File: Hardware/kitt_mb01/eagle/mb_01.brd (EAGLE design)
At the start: 160 x 100 mm, 123 parts, among them IC1.01 RT8293A, IC2.00 BQ24266RGET, IC3.01 LSM9DS1, U6.01 TPS61032RSARPSDO-G16, U7.01 SI1922EDH, U7.03 SI1922EDH, U7.2 SI1922EDH, X2.01 S2B-PH-K-S(LF)(SN), X7.02 ARDUINO_UNO, X7.03 CON_HEADER_1X02, X7.05 MOTOR, X7.06 CON_HEADER_1X02, X7.08 CON_HEADER_1X02, X7.09 0R-JUMPA, X7.10 0R-JUMPA, X7.11 CON_HEADER_1X02

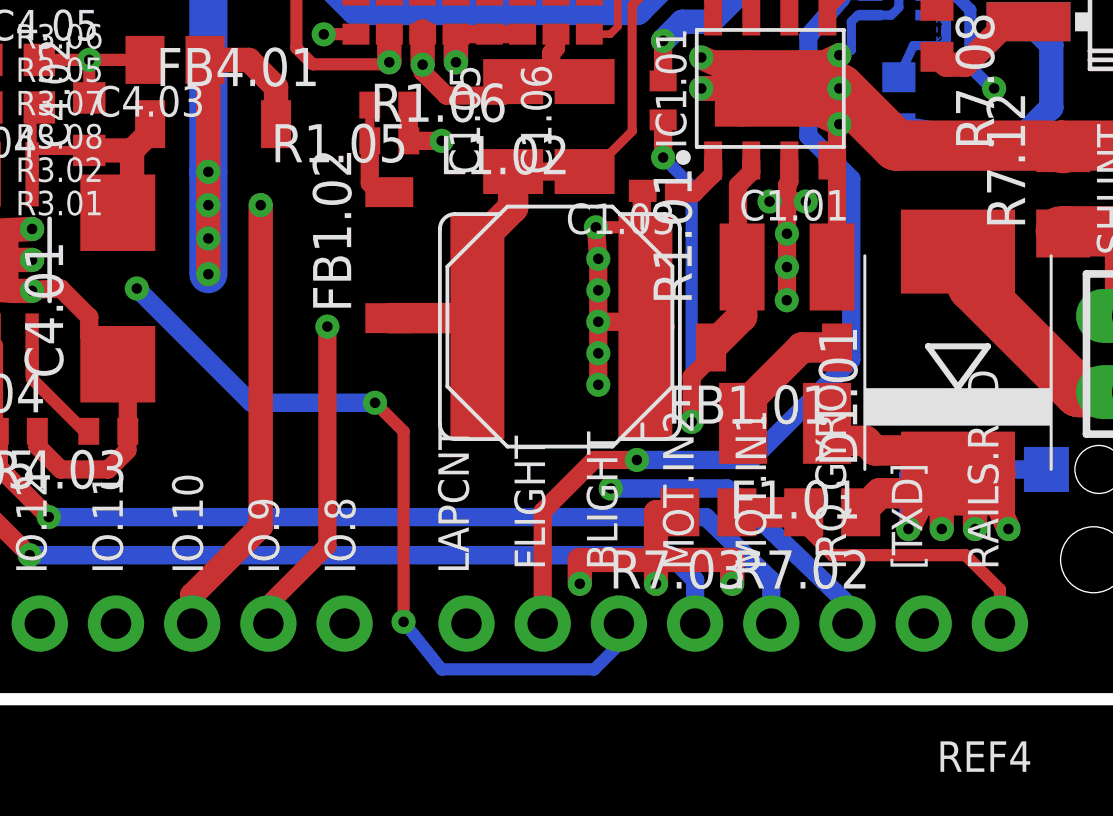
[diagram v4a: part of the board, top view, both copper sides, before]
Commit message: snapshot of mb-01 board -> double-checked pin usage between pcbs, needed to reroute one signal
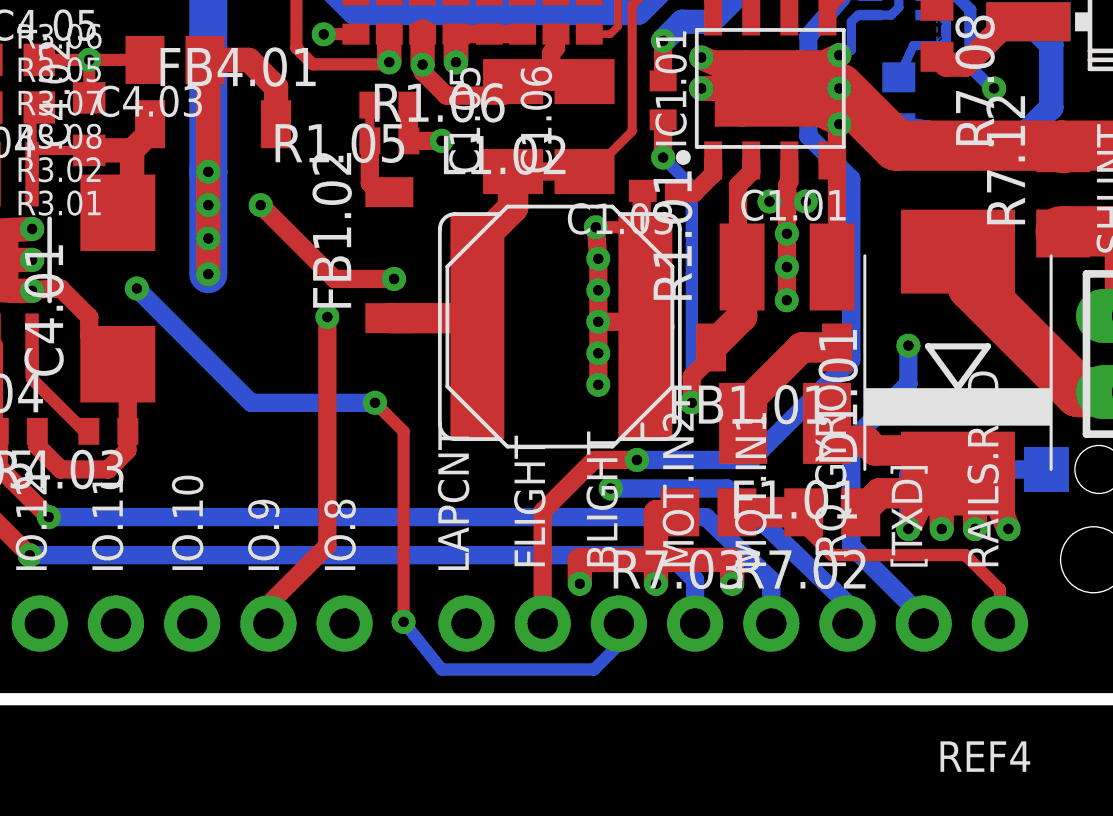
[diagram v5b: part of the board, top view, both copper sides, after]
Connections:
- net CAR.AUXILLARY: now also X7.02.IO.1; no longer X7.02.IO.10
- net GND: now also X7.02.GND.1
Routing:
- net CAR.AUXILLARY: track 40.2 -> 62.9 mm, vias 2 -> 4
- net N$81: track 20.9 -> 19.6 mm
- net CAR.GATECTLR: track 40.7 -> 41.2 mm
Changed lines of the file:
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@@
 <setting verticaltext="up"/>
 </settings>
-<grid distance="12.5" unitdist="mil" unit="mil" style="lines" multiple="1" display="yes" altdistance="0.0125" altunitdist="inch" altunit="inch"/>
+<grid distance="12.5" unitdist="mil" unit="mm" style="lines" multiple="1" display="yes" altdistance="0.0125" altunitdist="inch" altunit="inch"/>
 <layers>
 <layer number="1" name="Top" color="4" fill="1" visible="yes" active="yes"/>
@@
 <wire x1="68.73875" y1="57.388125" x2="67.071875" y2="58.26125" width="0.6096" layer="1"/>
 <wire x1="67.071875" y1="58.26125" x2="66.51625" y2="58.42" width="0.6096" layer="1"/>
+<contactref element="X7.02" pad="GND.1"/>
 <wire x1="83.740625" y1="41.1875" x2="84.455" y2="41.1875" width="0" layer="19" extent="1-1"/>
 <wire x1="62.215" y1="32.385" x2="62.23" y2="32.385" width="0" layer="19" extent="1-1"/>
@@
 <via x="87.074375" y="38.655625" extent="1-16" drill="0.35"/>
 <wire x1="87.074375" y1="38.655625" x2="88.026875" y2="37.703125" width="0.4064" layer="16"/>
-<wire x1="88.026875" y1="37.703125" x2="88.026875" y2="29.845" width="0.4064" layer="16"/>
-<via x="88.026875" y="29.845" extent="1-16" drill="0.35"/>
+<wire x1="88.026875" y1="37.703125" x2="88.026875" y2="30.48" width="0.4064" layer="16"/>
+<via x="88.026875" y="30.48" extent="1-16" drill="0.35"/>
 <wire x1="87.074375" y1="39.910625" x2="87.074375" y2="38.655625" width="0.6096" layer="1"/>
 <wire x1="88.67345" y1="32.323725" x2="89.70645" y2="33.356725" width="1.016" layer="1"/>
 <wire x1="89.70645" y1="33.356725" x2="89.70645" y2="35.0066" width="1.016" layer="1"/>
-<wire x1="88.026875" y1="29.845" x2="88.026875" y2="31.353125" width="0.6096" layer="1"/>
+<wire x1="88.026875" y1="30.48" x2="88.026875" y2="31.353125" width="0.6096" layer="1"/>
 <wire x1="88.026875" y1="31.353125" x2="88.5825" y2="31.90875" width="0.6096" layer="1"/>
 <wire x1="88.5825" y1="31.90875" x2="88.67345" y2="32.323725" width="0" layer="19" extent="1-1"/>
@@
 <wire x1="73.916" y1="23.12" x2="73.916" y2="23.751" width="0.6096" layer="1"/>
 <wire x1="73.916" y1="23.751" x2="75.8825" y2="25.7175" width="0.6096" layer="1"/>
-<wire x1="75.8825" y1="25.7175" x2="75.8825" y2="33.02" width="0.6096" layer="1"/>
-<via x="75.8825" y="33.02" extent="1-16" drill="0.35"/>
+<wire x1="75.8825" y1="25.7175" x2="75.8825" y2="33.3375" width="0.6096" layer="1"/>
+<via x="75.8825" y="33.3375" extent="1-16" drill="0.35"/>
 <via x="98.1075" y="40.9575" extent="1-16" drill="0.35"/>
 <wire x1="95.885" y1="38.735" x2="98.1075" y2="40.9575" width="0.6096" layer="3" curve="90"/>
@@
 <wire x1="89.931875" y1="39.21125" x2="87.391875" y2="39.84625" width="0.6096" layer="3" curve="3.565861"/>
 <wire x1="87.391875" y1="39.84625" x2="85.010625" y2="39.290625" width="0.6096" layer="3" curve="50.774725"/>
-<wire x1="85.010625" y1="39.290625" x2="75.8825" y2="33.02" width="0.6096" layer="3" curve="0.317259"/>
+<wire x1="77.47" y1="35.8775" x2="85.010625" y2="39.290625" width="0.6096" layer="3" curve="31.581671"/>
+<wire x1="77.47" y1="35.8775" x2="75.8825" y2="33.3375" width="0.6096" layer="3" curve="69.033193"/>
 </signal>
 <signal name="CAR.AUXILLARY">
 <contactref element="U7.2" pad="2"/>
-<contactref element="X7.02" pad="IO.10"/>
-<wire x1="71.376" y1="23.12" x2="71.376" y2="24.0685" width="0.8128" layer="1"/>
-<wire x1="71.376" y1="24.0685" x2="73.66" y2="26.3525" width="0.8128" layer="1"/>
 <wire x1="64.1622375" y1="52.86375" x2="60.6425" y2="52.86375" width="0.4064" layer="16"/>
 <wire x1="60.6425" y1="52.86375" x2="60.16625" y2="52.3875" width="0.4064" layer="16"/>
@@
 <wire x1="67.706875" y1="49.3191125" x2="64.1622375" y2="52.86375" width="0.4064" layer="16"/>
 <via x="73.66" y="37.068125" extent="1-16" drill="0.35"/>
-<wire x1="73.66" y1="37.068125" x2="73.66" y2="26.3525" width="0.8128" layer="1"/>
 <wire x1="73.66" y1="38.338125" x2="73.66" y2="37.068125" width="0.8128" layer="3"/>
 <wire x1="73.66" y1="38.338125" x2="67.78625" y2="49.2125" width="0.8128" layer="3" curve="61.251063"/>
+<contactref element="X7.02" pad="IO.1"/>
+<wire x1="95.76" y1="23.12" x2="95.76" y2="23.3025" width="0.6096" layer="16"/>
+<wire x1="95.76" y1="23.3025" x2="93.345" y2="25.7175" width="0.6096" layer="16"/>
+<wire x1="93.345" y1="25.7175" x2="93.345" y2="29.21" width="0.6096" layer="16"/>
+<wire x1="93.345" y1="29.21" x2="95.25" y2="31.115" width="0.6096" layer="16"/>
+<wire x1="95.25" y1="31.115" x2="95.25" y2="32.385" width="0.6096" layer="16"/>
+<via x="95.25" y="32.385" extent="1-16" drill="0.35"/>
+<wire x1="95.25" y1="32.385" x2="94.615" y2="33.02" width="0.6096" layer="3" curve="90"/>
+<wire x1="94.615" y1="33.02" x2="92.71" y2="32.0675" width="0.6096" layer="3" curve="53.130102"/>
+<wire x1="92.71" y1="32.0675" x2="88.5825" y2="28.2575" width="0.6096" layer="3" curve="-31.123015"/>
+<wire x1="88.5825" y1="28.2575" x2="87.3125" y2="28.8925" width="0.6096" layer="3" curve="-87.617023"/>
+<wire x1="87.3125" y1="28.8925" x2="86.0425" y2="29.5275" width="0.6096" layer="3" curve="87.617239"/>
+<wire x1="86.0425" y1="29.5275" x2="79.6925" y2="32.7025" width="0.6096" layer="3" curve="-92.108595"/>
+<wire x1="79.6925" y1="32.7025" x2="78.105" y2="34.6075" width="0.6096" layer="3" curve="75.990386"/>
+<via x="78.105" y="34.6075" extent="1-16" drill="0.35"/>
+<wire x1="78.105" y1="34.6075" x2="76.120625" y2="34.6075" width="0.6096" layer="1"/>
+<wire x1="76.120625" y1="34.6075" x2="73.66" y2="37.068125" width="0.6096" layer="1"/>
 </signal>
 </signals>

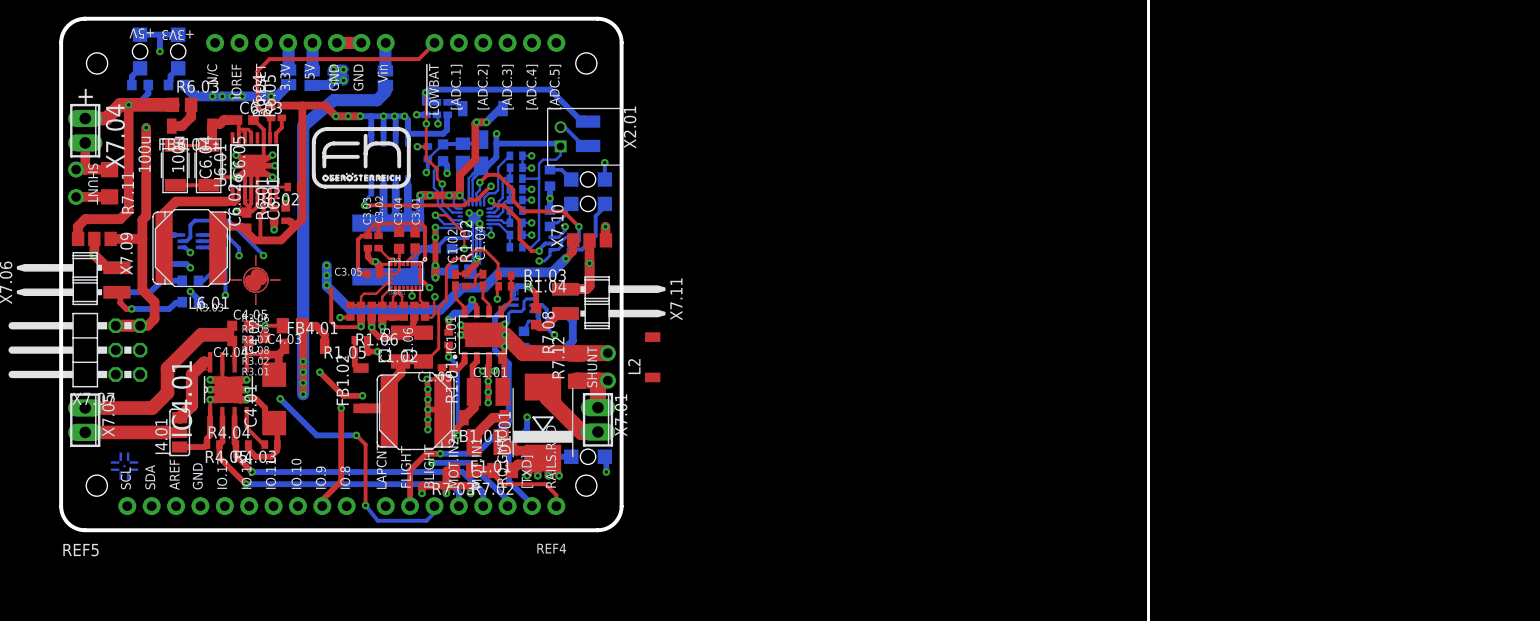
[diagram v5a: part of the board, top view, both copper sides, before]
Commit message: snapshot of mb01 board layout -> rearranged some vias -> minor reroutes were done -> started working on top silk layer
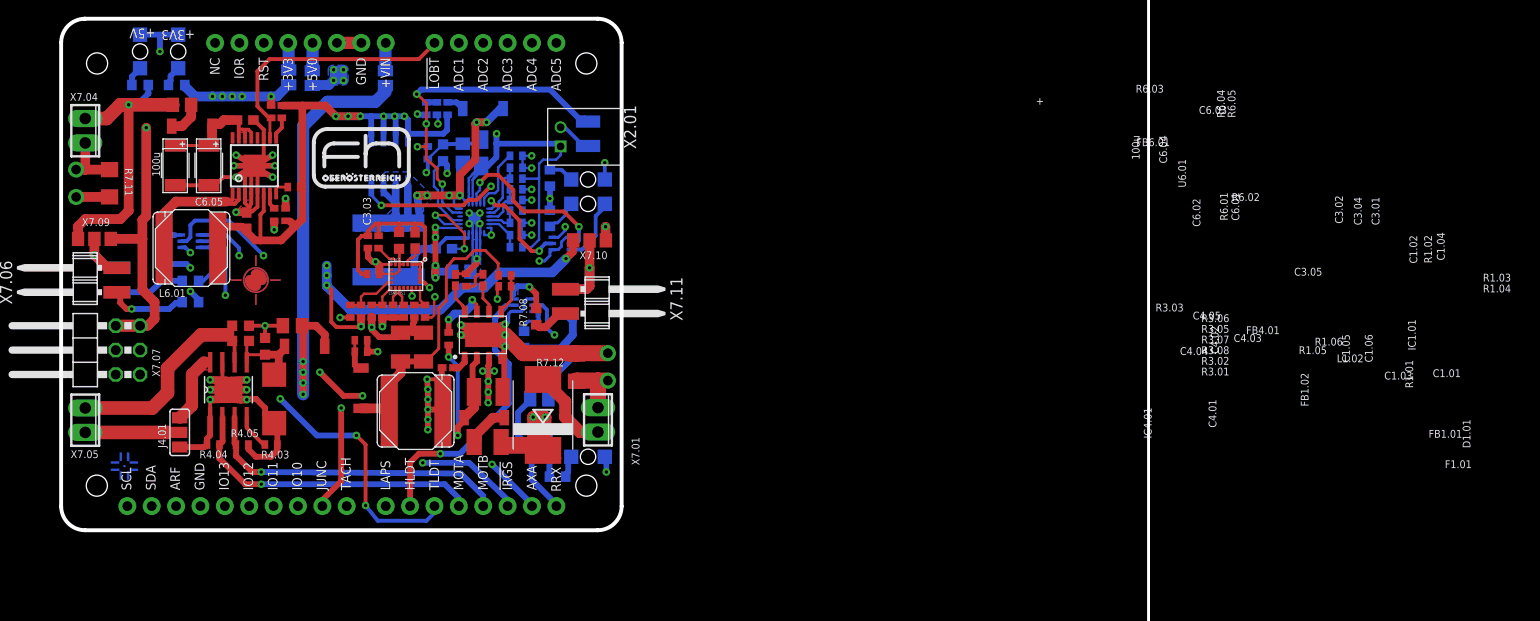
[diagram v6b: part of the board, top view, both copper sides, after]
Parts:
- removed L2: (no value), rcl:L4516C
- removed REF4: REF_GC-BBV2.0, kitt.con:REF_GHOSTCAR
- removed REF5: REF.KITT-MB01, kitt.refs:REF_KITT_MB01
- moved R7.03 10.9 mm to (96.5, 34.3), flipped to the bottom
- moved R7.02 4.55 mm to (96.7, 29.1), flipped to the bottom, turned to 0 degrees
- moved R7,05 2.92 mm to (98.4, 26.2)
- moved D1.01 0.79 mm to (96.9, 32.6)
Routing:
- net CAR.AUXILLARY: track 62.9 -> 52.4 mm
- net +12V: track 104.5 -> 110.1 mm
- net RAILS.RX: track 11.5 -> 13.6 mm
- net N$14: track 18.7 -> 17.1 mm
- net VCC/2: track 7.96 -> 8.95 mm
- net GND: track 246.1 -> 245.4 mm, vias 47 -> 44
- net CAR.FLIGHT: track 30.2 -> 29.6 mm
- net N$42: track 8.82 -> 8.30 mm
- added copper zone on layer 16, net N$18
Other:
- board text added: "!IRGS"
- board text added: "!LOBT"
- board text added: "+5V0"
- board text added: "+VIN"
- board text added: "ADC1"
- board text added: "ADC2"
- board text added: "ADC3"
- board text added: "ADC4"
- board text added: "ADC5"
- board text added: "ARF"
- board text added: "AXA"
- board text added: "GND"
- board text added: "HLDT"
- board text added: "IO10"
- board text added: "IO11"
- board text added: "IO12"
- board text added: "IO13"
- board text added: "IOR"
- board text added: "JUNC"
- board text added: "LAPS"
- board text added: "MOTA"
- board text added: "MOTB"
- board text added: "NC"
- board text added: "RRX"
- board text added: "RST"
- board text added: "SCL"
- board text added: "SDA"
- board text added: "TACH"
- board text added: "TLDT"
- board text removed: "GROUND POURS"
- board text removed: "RAILS POURS"
- board text removed: "SHUNT"
- board text removed: "TEST COUPON on PANELIZING -> include layer indicator and fiducial marks -> can include spare headlight -> even a I2C or decatron knightrider blinkenlight would be an option here"
- board text removed: "TODO: COMMAND/BOTTOM LIGHT!!!"

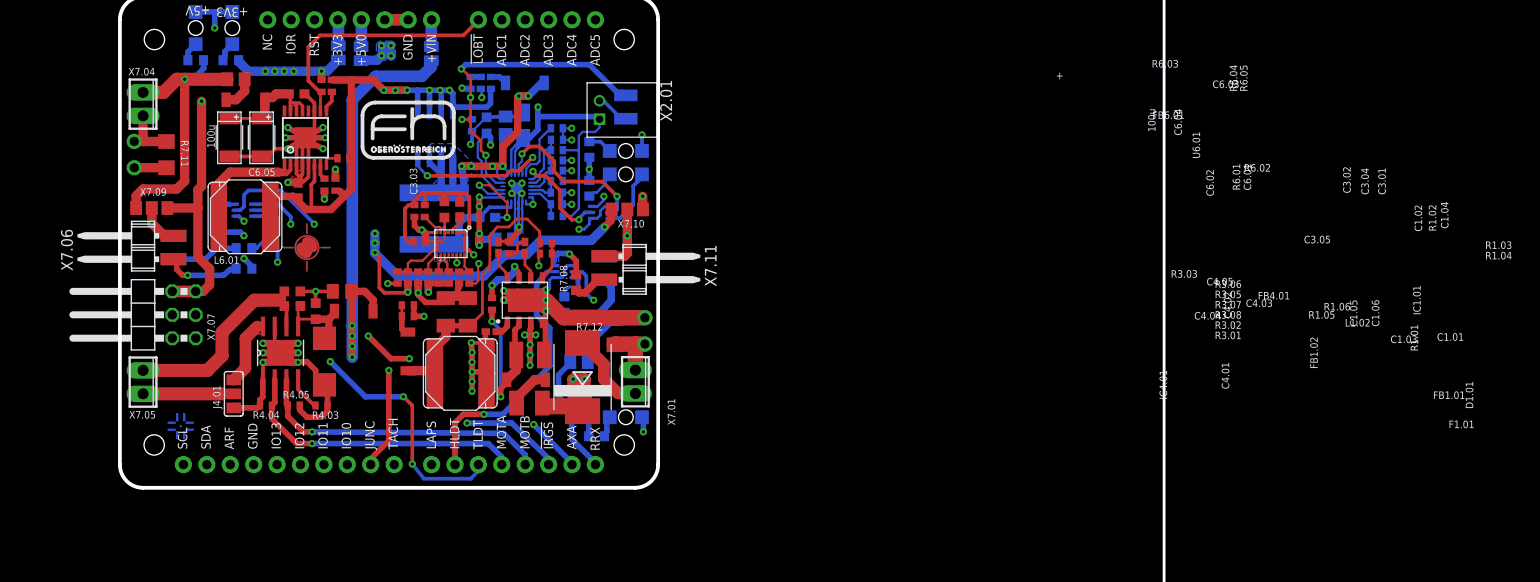
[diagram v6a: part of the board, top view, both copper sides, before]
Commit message: snapshot of mb01 board layout -> did majority of top silk names, values have been deleted    because there's not enough time for such things
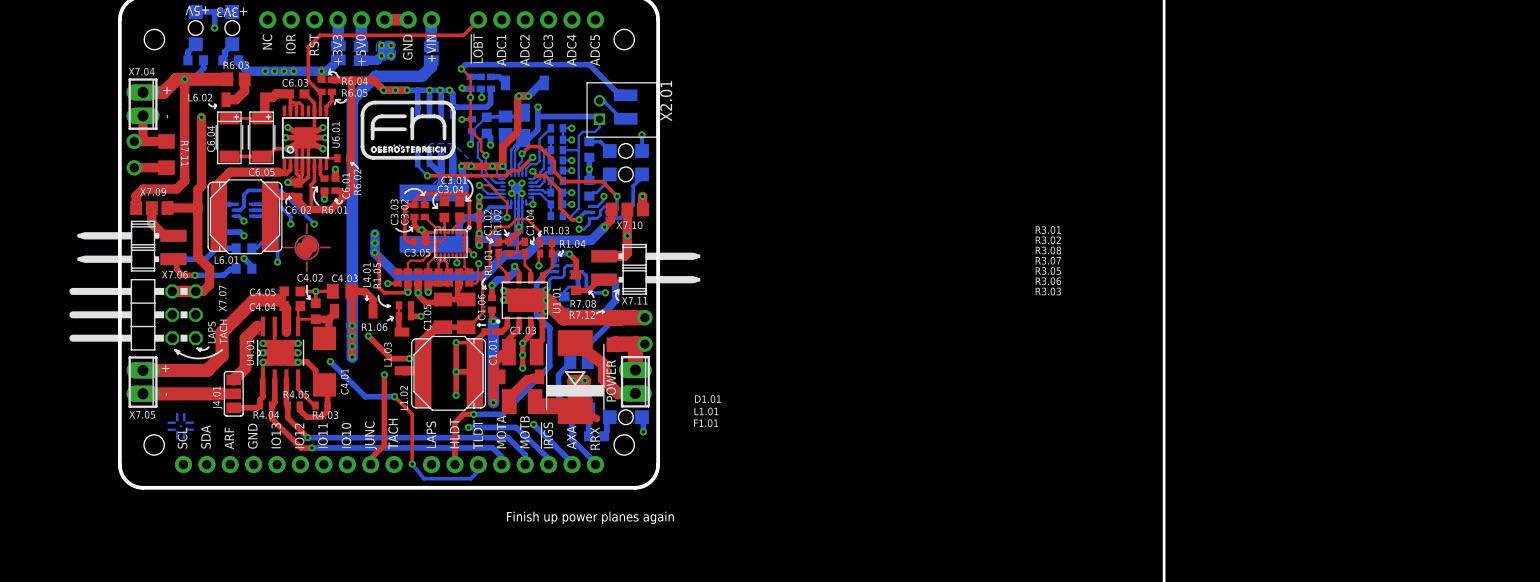
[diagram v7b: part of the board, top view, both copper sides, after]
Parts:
- removed FB1.01, FB1.02: BEAD, rcl:L4516C
- added L1.01, L1.03: BEAD, rcl:L4516C
- moved L1.02 1.27 mm to (82.2, 33.0)
- moved C1.01 0.85 mm to (90.4, 35.3)
- moved F1.01 0.81 mm to (90.3, 30.0)
- moved D1.01 0.79 mm to (96.1, 32.6)
- moved C1.05 0.35 mm to (81.8, 39.5)
- moved R1.05 0.32 mm to (77.6, 40.4)
- moved R1.06 0.32 mm to (77.6, 39.2)
- moved C1.06 0.22 mm to (84.3, 39.5)
- renumbered FB4.01 to L4.01, FB6.01 to L6.02, IC1.01 to U1.01, IC4.01 to U4.01
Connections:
- net N$80: now also L1.01.1; no longer FB1.01.1
- net N$81: now also L1.01.2; no longer FB1.01.2
- net N$87: now also L1.03.1; no longer FB1.02.1
- net N$90: now also L1.03.2; no longer FB1.02.2
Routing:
- net +12V: track 110.1 -> 112.2 mm
- net CAR.GATECTLR: track 41.2 -> 43.2 mm
- net N$81: track 19.6 -> 21.5 mm
- net N$42: track 8.30 -> 9.51 mm
- net N$87: track 31.0 -> 32.1 mm
- net CAR.AUXILLARY: track 52.4 -> 53.5 mm
- net +3V3: track 161.6 -> 160.7 mm
- net N$33: track 24.6 -> 25.4 mm
- net VCC/2: track 8.95 -> 9.55 mm
- net CAR.BLIGHT: track 46.3 -> 45.8 mm
- net N$88: track 18.0 -> 17.4 mm, vias 11 -> 6
- net !IRQ_GYRO: track 39.9 -> 40.5 mm
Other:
- board text added: "-"
- board text added: "Finish up power planes again"
- board text added: "POWER"
- board text removed: "SpeedBoard--> Lap Detector-->"
